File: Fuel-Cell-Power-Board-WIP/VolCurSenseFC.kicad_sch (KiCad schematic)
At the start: 6 parts, among them U10 TSV912IDT, U7 ACS770xCB-050B-PFF

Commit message: Commit
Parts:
- added C20: 0.1uF, symbol Device:C
- added unit 3 of U7
- added unit 2 of U7
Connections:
- net +5V: now also C20.2, U7.8 (V+)
- net Current_Meas: now also U7.5 (+)
- net Current_Sense_IN: now also R16.1; no longer R15.2
- net GND: now also R15.1, C20.1, U7.4 (V-); no longer R16.2
- net Voltage_Meas: no longer D17.1 (K)
- new net: D17.1 (K), R15.2, R16.2, U10.3 (+)
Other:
- note added: "12 bit ADC Vref = 3.3V 000000000000 3.3V/2^12 = 0.805mV * 1A / 185mV = 4mA 1V -> 1.00805V"
- note added: "28V"
- note added: "3.3V"
- note added: "For the FC power, we expect: VIN_MAX = 28V Maximum input voltage == VOUT to MCU pin: 4.0V Design for VOUT = 3.3V VOUT = R2/(R1+R2) * VIN 3.3V = R2/(R1+R2) * 28V R1 = 7.48R2 Use standard resistors of R2 = 1k R1 = 7.5k"
- note removed: "For the FC power, we expect: VIN_MAX = 28V Maximum input voltage == VOUT to MCU pin: 4.0V Design for VOUT = 3.3V VOUT = R2/(R1+R2) * VIN 3.3V = R2/(R1+R2) * 28V R1 = 7.48R2 Use standard resistors of R1 = 1k R2 = 7.5k"
- moved on the sheet: D17, R15, R16, U10A

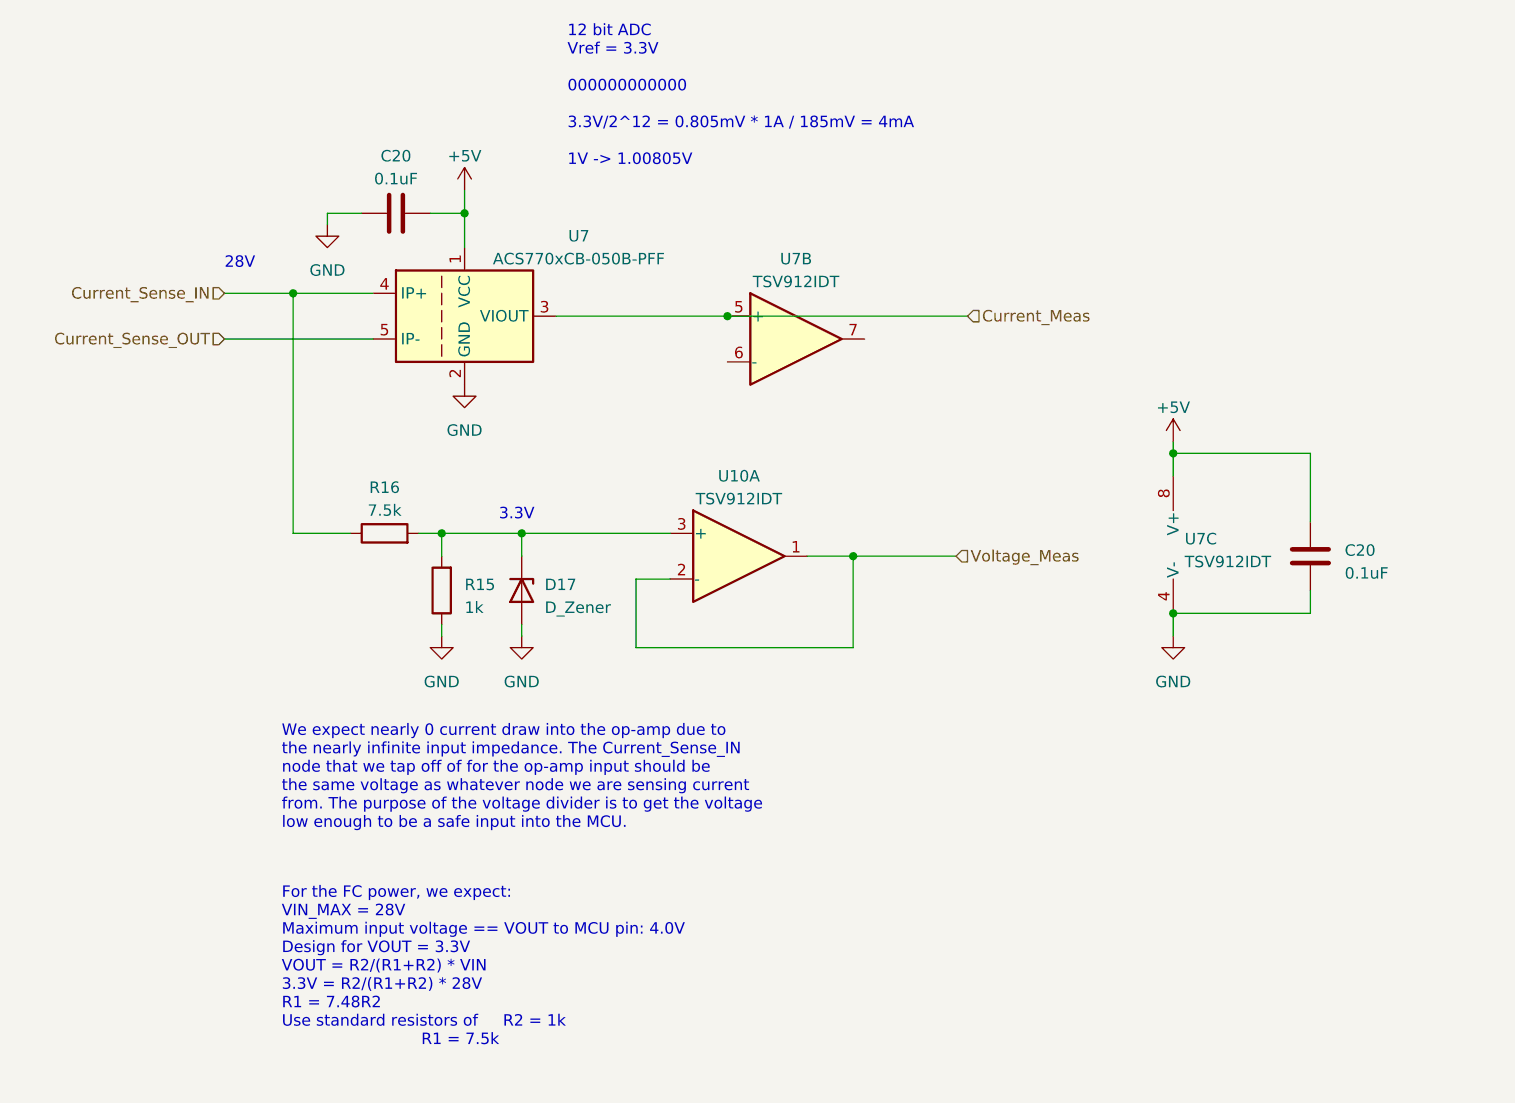
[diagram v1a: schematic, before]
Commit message: Major changes: removed 12V reg, added battery power for 5V/12V, revised current sensing modules to have a smaller upper limit, added voltage divider + op-amp for more measurements.
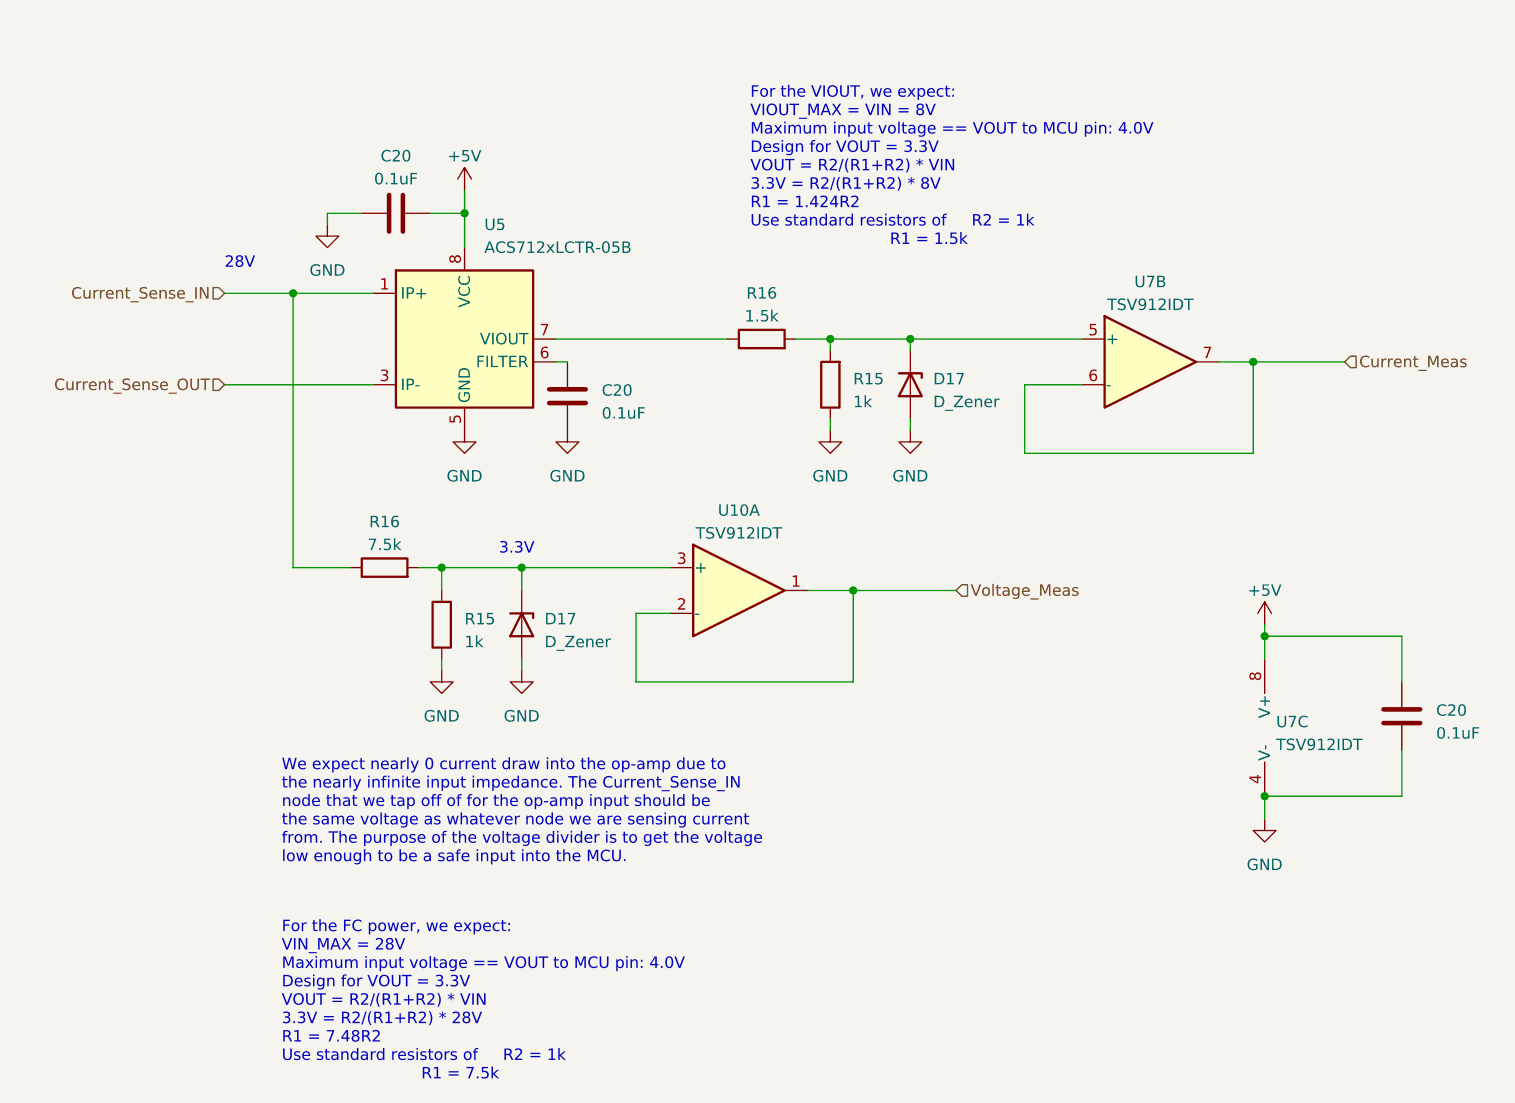
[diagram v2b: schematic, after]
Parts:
- removed unit 1 of U7
- added C20: 0.1uF, symbol Device:C
- added D17: D_Zener, symbol Device:D_Zener
- added R15: 1k, symbol Device:R
- added R16: 1.5k, symbol Device:R
- added U5: ACS712xLCTR-05B, Package_SO:SOIC-8_3.9x4.9mm_P1.27mm, symbol Sensor_Current:ACS712xLCTR-05B
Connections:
- net +5V: now also U5.8 (VCC)
- net Current_Meas: now also U7.6 (-), U7.7; no longer U7.5 (+)
- net Current_Sense_IN: now also U5.1 (IP+), U5.2 (IP+)
- net Current_Sense_OUT: now also U5.3 (IP-), U5.4 (IP-)
- net GND: now also C20.1, D17.2 (A), R15.1, U5.5 (GND)
- new net: C20.2, U5.6 (FILTER)
- new net: R16.1, U5.7 (VIOUT)
- new net: D17.1 (K), R15.2, R16.2, U7.5 (+)
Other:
- note added: "For the VIOUT, we expect: VIOUT_MAX = VIN = 8V Maximum input voltage == VOUT to MCU pin: 4.0V Design for VOUT = 3.3V VOUT = R2/(R1+R2) * VIN 3.3V = R2/(R1+R2) * 8V R1 = 1.424R2 Use standard resistors of R2 = 1k R1 = 1.5k"
- note removed: "12 bit ADC Vref = 3.3V 000000000000 3.3V/2^12 = 0.805mV * 1A / 185mV = 4mA 1V -> 1.00805V"
- moved on the sheet: C20, D17, R15, R16, U10A, U7B, U7C

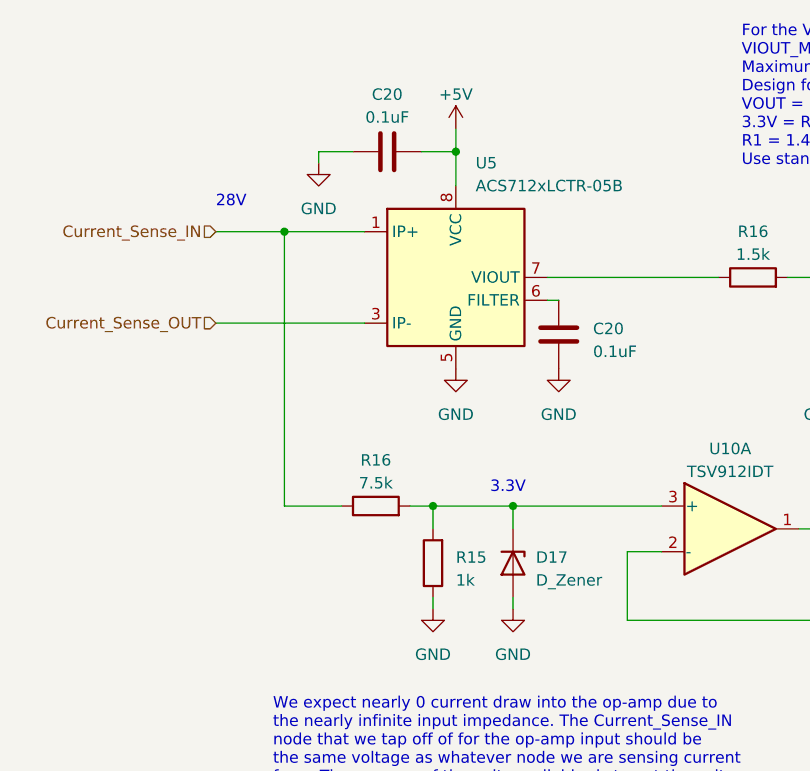
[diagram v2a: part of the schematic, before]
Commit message: made changes to Power flow stuff
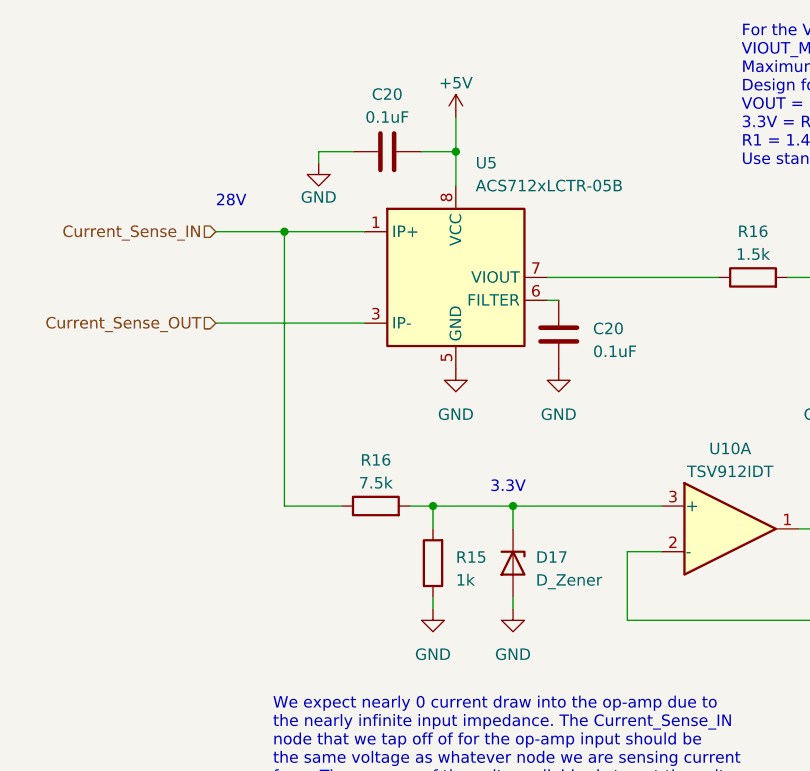
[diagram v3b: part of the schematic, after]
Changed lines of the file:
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@@
-    (stroke (width 0) (type default))
-  )
-  (wire (pts (xy 74.93 105.41) (xy 74.93 106.68))
     (stroke (width 0) (type default))
   )
@@
     (stroke (width 0) (type default))
   )
-  (wire (pts (xy 68.58 53.34) (xy 68.58 55.88))
+  (wire (pts (xy 68.58 52.07) (xy 68.58 55.88))
     (stroke (width 0) (type default))
   )
@@
   )
   (wire (pts (xy 172.72 102.87) (xy 172.72 107.95))
+    (stroke (width 0) (type default))
+  )
+  (wire (pts (xy 74.93 106.68) (xy 74.93 105.41))
     (stroke (width 0) (type default))
   )
@@
     )
   )
-  (symbol (lib_id "power:+5V") (at 68.58 53.34 0) (unit 1)
-    (in_bom yes) (on_board yes) (dnp no) (fields_autoplaced)
-    (property "Reference" "#PWR031" (at 68.58 57.15 0)
-      (effects (font (size 1.27 1.27)) hide)
-    )
-    (property "Value" "+5V" (at 68.58 49.53 0)
-      (effects (font (size 1.27 1.27)))
-    )
-    (property "Footprint" "" (at 68.58 53.34 0)
-      (effects (font (size 1.27 1.27)) hide)
-    )
-    (property "Datasheet" "" (at 68.58 53.34 0)
+  (symbol (lib_id "power:+5V") (at 68.58 52.07 0) (unit 1)
+    (in_bom yes) (on_board yes) (dnp no) (fields_autoplaced)
+    (property "Reference" "#PWR031" (at 68.58 55.88 0)
+      (effects (font (size 1.27 1.27)) hide)
+    )
+    (property "Value" "+5V" (at 68.58 48.26 0)
+      (effects (font (size 1.27 1.27)))
+    )
+    (property "Footprint" "" (at 68.58 52.07 0)
+      (effects (font (size 1.27 1.27)) hide)
+    )
+    (property "Datasheet" "" (at 68.58 52.07 0)
       (effects (font (size 1.27 1.27)) hide)
     )
@@
   )
   (symbol (lib_id "power:GND") (at 53.34 57.15 0) (unit 1)
-    (in_bom yes) (on_board yes) (dnp no) (fields_autoplaced)
+    (in_bom yes) (on_board yes) (dnp no)
     (property "Reference" "#PWR030" (at 53.34 63.5 0)
       (effects (font (size 1.27 1.27)) hide)
     )
-    (property "Value" "GND" (at 53.34 62.23 0)
-      (effects (font (size 1.27 1.27)))
-    )
+    (property "Value" "GND" (at 53.34 60.96 0)
+      (effects (font (size 1.27 1.27)))
+    )
